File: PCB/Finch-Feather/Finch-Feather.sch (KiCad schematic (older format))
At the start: 37 parts, among them M1 STM32WB5MMGH6TR, Q1 DMP3125L-7, SW1 B3U-1000P, T1 20021121-00010C4LF, T2 TSW-112-07-G-S, T3 DX07S016JA1R1500, T4 TSW-116-07-L-S, T5 S2B-PH-SM4-TB(LF)(SN), U1 USBLC6-2P6, U2 TLV75533PDBVR, U3 MCP73831T-2ACI_OT

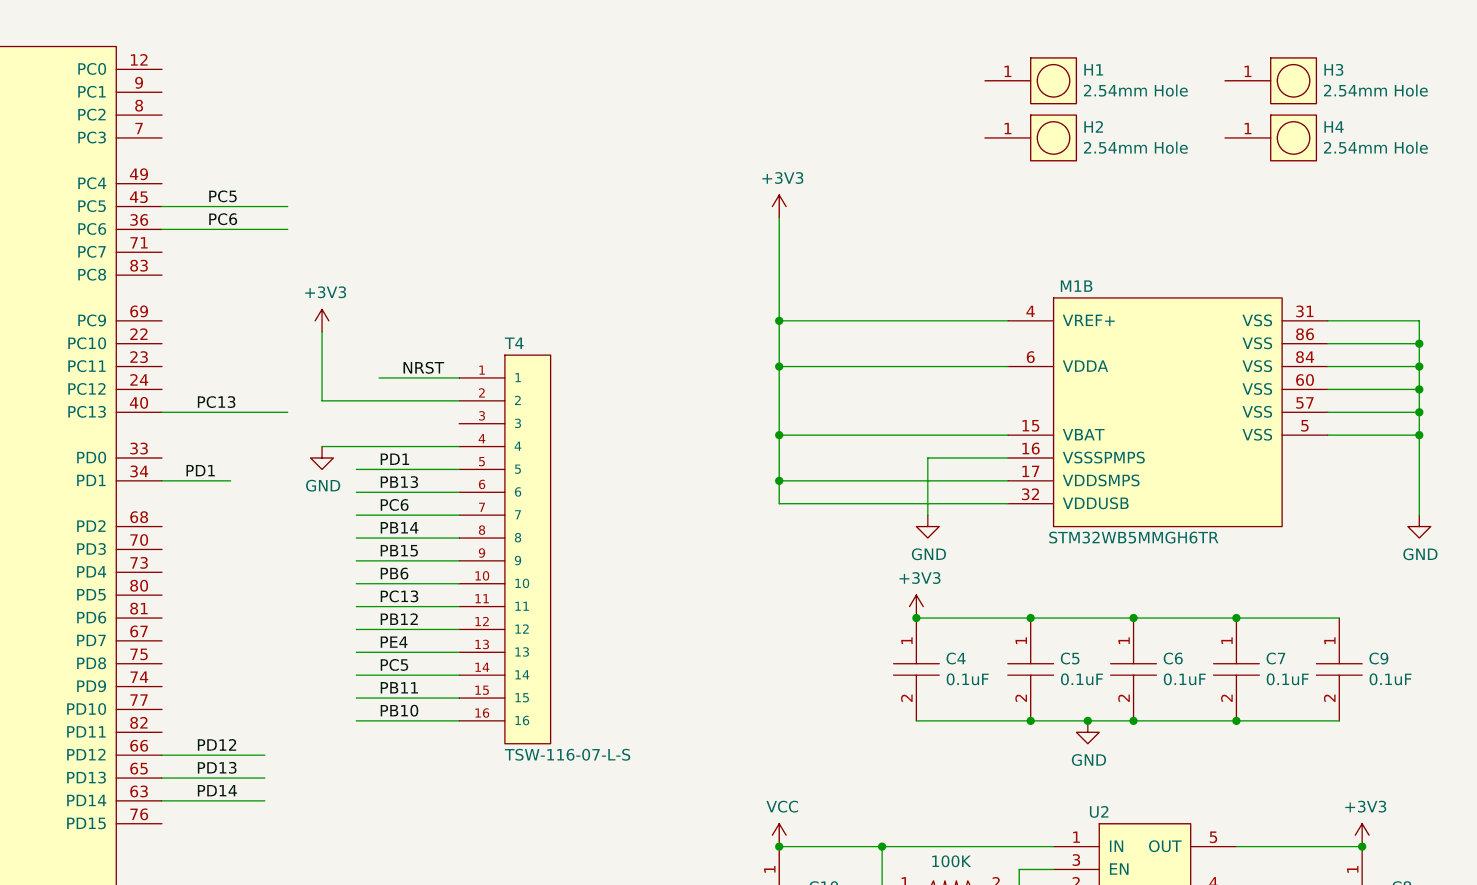
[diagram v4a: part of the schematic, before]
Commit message: Heavy PCB Rework
Reworked the Portion of the PCB around the ST RF module, signals re-chosen for 3 GPIOs to make the grounding conform more to the reference design recommendations.
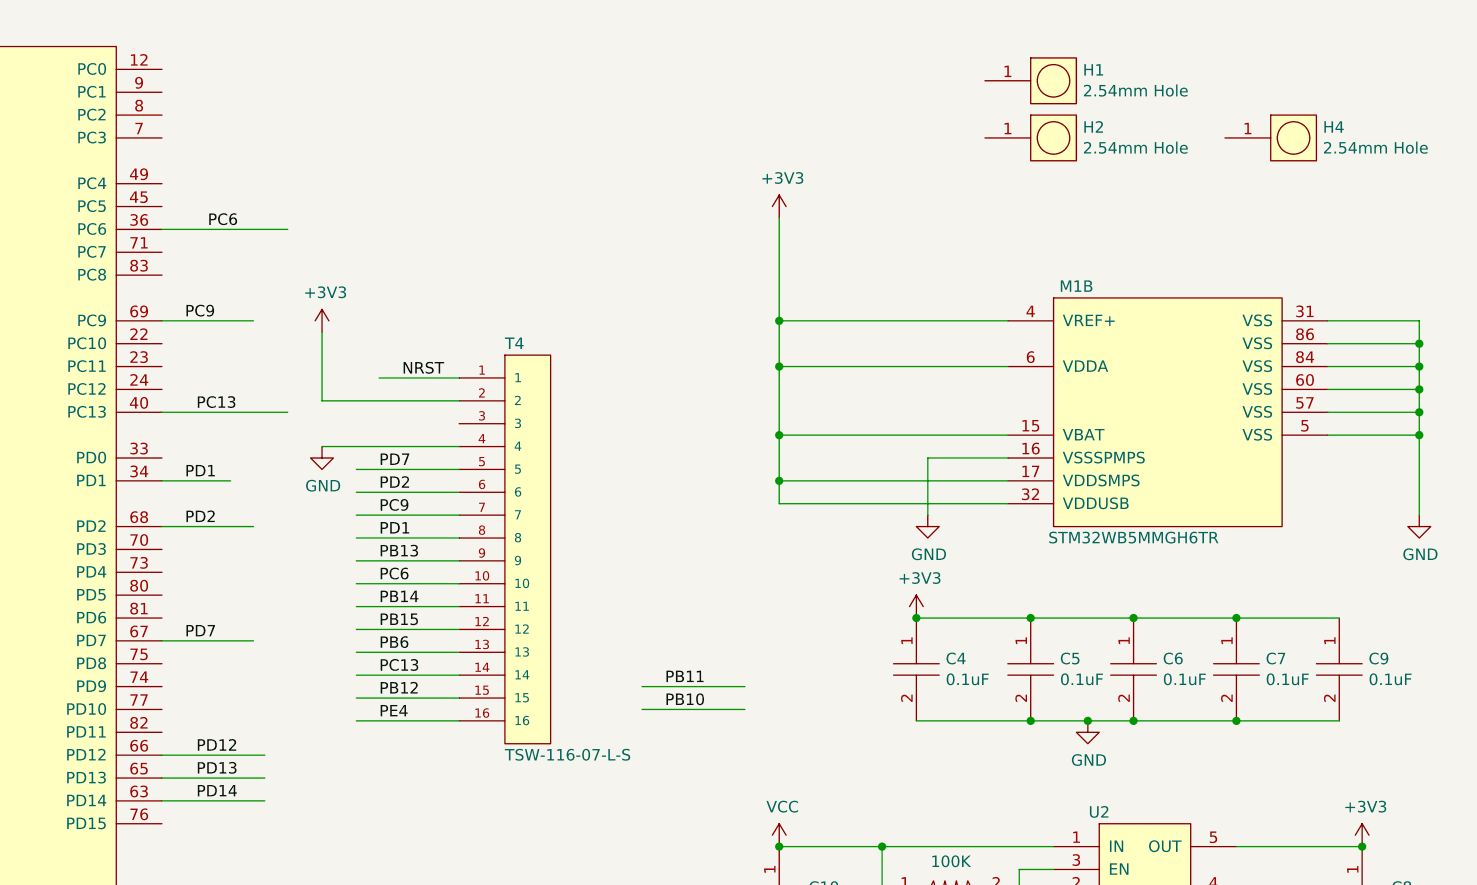
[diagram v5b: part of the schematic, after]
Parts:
- removed H3: 2.54mm_PLT_Hole, AVR-KiCAD-Lib-Holes_Fasteners:2.54mm_PLT_Hole, symbol AVR-KiCAD-Lib-Holes_Fasteners:2.54mm_PLT_Hole
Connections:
- net labels added: PC9, PD2, PD7
- net labels removed: PC5
- wire segments 171 -> 175
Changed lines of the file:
@@
-$EndComp
-$Comp
-L AVR-KiCAD-Lib-Holes_Fasteners:2.54mm_PLT_Hole H3
-U 1 1 608C5DF9
-P 10400 900
-F 0 "H3" H 10628 946 50  0000 L CNN
-F 1 "2.54mm_PLT_Hole" H 10450 1100 50  0001 C CNN
-F 2 "AVR-KiCAD-Lib-Holes_Fasteners:2.54mm_PLT_Hole" H 10400 900 50  0001 C CNN
-F 3 "" H 10400 900 50  0001 C CNN
-F 4 "*" H 10500 1150 50  0001 C CNN "Cost QTY: 1"
-F 5 "*" H 10600 1250 50  0001 C CNN "Cost QTY: 1000"
-F 6 "*" H 10700 1350 50  0001 C CNN "Cost QTY: 2500"
-F 7 "*" H 10800 1450 50  0001 C CNN "Cost QTY: 5000"
-F 8 "*" H 10900 1550 50  0001 C CNN "Cost QTY: 10000"
-F 9 "*" H 11000 1650 50  0001 C CNN "MFR"
-F 10 "*" H 11100 1750 50  0001 C CNN "MFR#"
-F 11 "*" H 11200 1850 50  0001 C CNN "Vendor"
-F 12 "*" H 11300 1950 50  0001 C CNN "Vendor #"
-F 13 "*" H 11400 2050 50  0001 C CNN "Designer"
-F 14 "*" H 11500 2150 50  0001 C CNN "Height"
-F 15 "*" H 12600 3250 50  0001 C CNN "Date Created"
-F 16 "*" H 11600 2250 50  0001 C CNN "Date Modified"
-F 17 "*" H 11700 2350 50  0001 C CNN "Lead-Free ?"
-F 18 "*" H 11800 2450 50  0001 C CNN "RoHS Levels"
-F 19 "*" H 11900 2550 50  0001 C CNN "Mounting"
-F 20 "*" H 12000 2650 50  0001 C CNN "Pin Count #"
-F 21 "*" H 12100 2750 50  0001 C CNN "Status"
-F 22 "*" H 12200 2850 50  0001 C CNN "Tolerance"
-F 23 "*" H 12300 2950 50  0001 C CNN "Type"
-F 24 "*" H 12400 3050 50  0001 C CNN "Voltage"
-F 25 "*" H 12500 3200 50  0001 C CNN "Package"
-F 26 "2.54mm Hole" H 10628 855 50  0000 L CNN "_Value_"
-F 27 "*" H 12800 3500 50  0001 C CNN "Management_ID"
-F 28 "*" H 12800 3500 50  0001 C CNN "Description"
-	1    10400 900
-	1    0    0    -1
 $EndComp
 $Comp
@@
 PB10
 Wire Wire Line
-	6850 3700 6400 3700
-Text Label 6500 3700 0    50   ~ 0
+	8100 3650 7650 3650
+Text Label 7750 3650 0    50   ~ 0
 PB10
 Wire Wire Line
@@
 PB11
 Wire Wire Line
-	6850 3600 6400 3600
-Text Label 6500 3600 0    50   ~ 0
+	8100 3550 7650 3550
+Text Label 7750 3550 0    50   ~ 0
 PB11
-Text Label 5750 1450 0    50   ~ 0
-PC5
-Wire Wire Line
-	5550 1450 6100 1450
-Text Label 6500 3500 0    50   ~ 0
-PC5
-Wire Wire Line
-	6400 3500 6850 3500
 Wire Wire Line
 	5550 5050 6050 5050
@@
 PE4
 Wire Wire Line
-	6400 3400 6850 3400
-Text Label 6500 3400 0    50   ~ 0
+	6400 3700 6850 3700
+Text Label 6500 3700 0    50   ~ 0
 PE4
 Wire Wire Line
@@
 PB12
 Wire Wire Line
-	6850 3300 6400 3300
-Text Label 6500 3300 0    50   ~ 0
+	6850 3600 6400 3600
+Text Label 6500 3600 0    50   ~ 0
 PB12
 Wire Wire Line
@@
 PC13
 Wire Wire Line
-	6850 3200 6400 3200
-Text Label 6500 3200 0    50   ~ 0
+	6850 3500 6400 3500
+Text Label 6500 3500 0    50   ~ 0
 PC13
 Wire Wire Line
@@
 PB6
 Wire Wire Line
-	6850 3100 6400 3100
-Text Label 6500 3100 0    50   ~ 0
+	6850 3400 6400 3400
+Text Label 6500 3400 0    50   ~ 0
 PB6
 Wire Wire Line
@@
 PB15
 Wire Wire Line
-	6850 3000 6400 3000
-Text Label 6500 3000 0    50   ~ 0
+	6850 3300 6400 3300
+Text Label 6500 3300 0    50   ~ 0
 PB15
 Wire Wire Line
@@
 PB14
 Wire Wire Line
-	6850 2900 6400 2900
-Text Label 6500 2900 0    50   ~ 0
+	6850 3200 6400 3200
+Text Label 6500 3200 0    50   ~ 0
 PB14
 Wire Wire Line
@@
 PC6
 Wire Wire Line
-	6400 2800 6850 2800
-Text Label 6500 2800 0    50   ~ 0
+	6400 3100 6850 3100
+Text Label 6500 3100 0    50   ~ 0
 PC6
 Wire Wire Line
@@
 PB13
 Wire Wire Line
-	6400 2700 6850 2700
-Text Label 6500 2700 0    50   ~ 0
+	6400 3000 6850 3000
+Text Label 6500 3000 0    50   ~ 0
 PB13
 Wire Wire Line
@@
 PD1
 Wire Wire Line
-	6400 2600 6850 2600
-Text Label 6500 2600 0    50   ~ 0
+	6400 2900 6850 2900
+Text Label 6500 2900 0    50   ~ 0
 PD1
 Wire Wire Line
@@
 Wire Wire Line
 	9100 5450 9100 6250
+Wire Wire Line
+	5550 3350 5950 3350
+Text Label 5650 3350 0    50   ~ 0
+PD7
+Wire Wire Line
+	6400 2600 6850 2600
+Text Label 6500 2600 0    50   ~ 0
+PD7
+Wire Wire Line
+	5550 2850 5950 2850
+Text Label 5650 2850 0    50   ~ 0
+PD2
+Wire Wire Line
+	6400 2700 6850 2700
+Text Label 6500 2700 0    50   ~ 0
+PD2
+Wire Wire Line
+	5550 1950 5950 1950
+Text Label 5650 1950 0    50   ~ 0
+PC9
+Wire Wire Line
+	6400 2800 6850 2800
+Text Label 6500 2800 0    50   ~ 0
+PC9
 $EndSCHEMATC

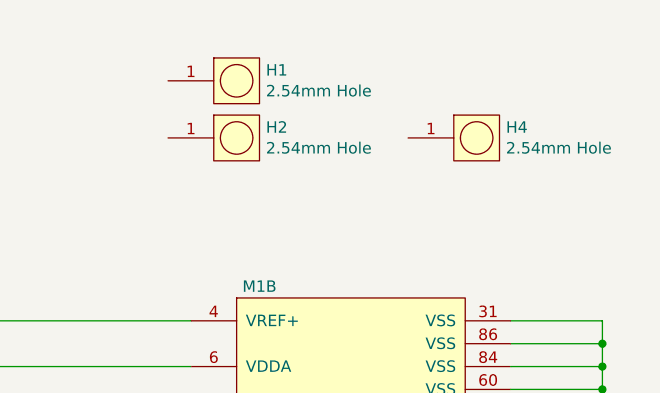
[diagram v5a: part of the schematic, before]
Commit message: Prefab changes
minor adjustments, removal of screw holes, and additional via stitching
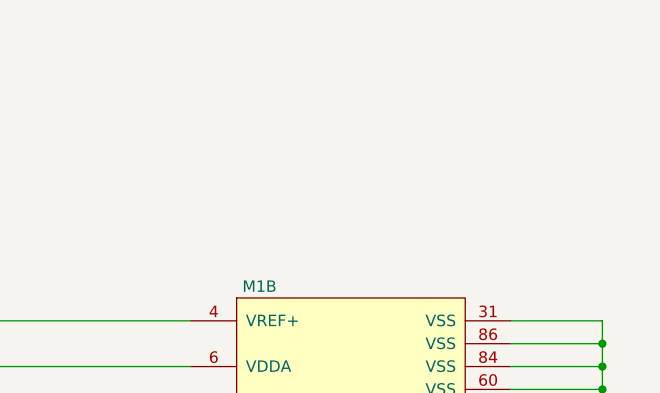
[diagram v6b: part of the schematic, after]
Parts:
- removed H1, H2, H4: 2.54mm_PLT_Hole, AVR-KiCAD-Lib-Holes_Fasteners:2.54mm_PLT_Hole, symbol AVR-KiCAD-Lib-Holes_Fasteners:2.54mm_PLT_Hole
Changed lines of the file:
@@
-$EndComp
-$Comp
-L AVR-KiCAD-Lib-Holes_Fasteners:2.54mm_PLT_Hole H1
-U 1 1 608C1076
-P 9350 900
-F 0 "H1" H 9578 946 50  0000 L CNN
-F 1 "2.54mm_PLT_Hole" H 9400 1100 50  0001 C CNN
-F 2 "AVR-KiCAD-Lib-Holes_Fasteners:2.54mm_PLT_Hole" H 9350 900 50  0001 C CNN
-F 3 "" H 9350 900 50  0001 C CNN
-F 4 "*" H 9450 1150 50  0001 C CNN "Cost QTY: 1"
-F 5 "*" H 9550 1250 50  0001 C CNN "Cost QTY: 1000"
-F 6 "*" H 9650 1350 50  0001 C CNN "Cost QTY: 2500"
-F 7 "*" H 9750 1450 50  0001 C CNN "Cost QTY: 5000"
-F 8 "*" H 9850 1550 50  0001 C CNN "Cost QTY: 10000"
-F 9 "*" H 9950 1650 50  0001 C CNN "MFR"
-F 10 "*" H 10050 1750 50  0001 C CNN "MFR#"
-F 11 "*" H 10150 1850 50  0001 C CNN "Vendor"
-F 12 "*" H 10250 1950 50  0001 C CNN "Vendor #"
-F 13 "*" H 10350 2050 50  0001 C CNN "Designer"
-F 14 "*" H 10450 2150 50  0001 C CNN "Height"
-F 15 "*" H 11550 3250 50  0001 C CNN "Date Created"
-F 16 "*" H 10550 2250 50  0001 C CNN "Date Modified"
-F 17 "*" H 10650 2350 50  0001 C CNN "Lead-Free ?"
-F 18 "*" H 10750 2450 50  0001 C CNN "RoHS Levels"
-F 19 "*" H 10850 2550 50  0001 C CNN "Mounting"
-F 20 "*" H 10950 2650 50  0001 C CNN "Pin Count #"
-F 21 "*" H 11050 2750 50  0001 C CNN "Status"
-F 22 "*" H 11150 2850 50  0001 C CNN "Tolerance"
-F 23 "*" H 11250 2950 50  0001 C CNN "Type"
-F 24 "*" H 11350 3050 50  0001 C CNN "Voltage"
-F 25 "*" H 11450 3200 50  0001 C CNN "Package"
-F 26 "2.54mm Hole" H 9578 855 50  0000 L CNN "_Value_"
-F 27 "*" H 11750 3500 50  0001 C CNN "Management_ID"
-F 28 "*" H 11750 3500 50  0001 C CNN "Description"
-	1    9350 900
-	1    0    0    -1
-$EndComp
-$Comp
-L AVR-KiCAD-Lib-Holes_Fasteners:2.54mm_PLT_Hole H2
-U 1 1 608C3B0F
-P 9350 1150
-F 0 "H2" H 9578 1196 50  0000 L CNN
-F 1 "2.54mm_PLT_Hole" H 9400 1350 50  0001 C CNN
-F 2 "AVR-KiCAD-Lib-Holes_Fasteners:2.54mm_PLT_Hole" H 9350 1150 50  0001 C CNN
-F 3 "" H 9350 1150 50  0001 C CNN
-F 4 "*" H 9450 1400 50  0001 C CNN "Cost QTY: 1"
-F 5 "*" H 9550 1500 50  0001 C CNN "Cost QTY: 1000"
-F 6 "*" H 9650 1600 50  0001 C CNN "Cost QTY: 2500"
-F 7 "*" H 9750 1700 50  0001 C CNN "Cost QTY: 5000"
-F 8 "*" H 9850 1800 50  0001 C CNN "Cost QTY: 10000"
-F 9 "*" H 9950 1900 50  0001 C CNN "MFR"
-F 10 "*" H 10050 2000 50  0001 C CNN "MFR#"
-F 11 "*" H 10150 2100 50  0001 C CNN "Vendor"
-F 12 "*" H 10250 2200 50  0001 C CNN "Vendor #"
-F 13 "*" H 10350 2300 50  0001 C CNN "Designer"
-F 14 "*" H 10450 2400 50  0001 C CNN "Height"
-F 15 "*" H 11550 3500 50  0001 C CNN "Date Created"
-F 16 "*" H 10550 2500 50  0001 C CNN "Date Modified"
-F 17 "*" H 10650 2600 50  0001 C CNN "Lead-Free ?"
-F 18 "*" H 10750 2700 50  0001 C CNN "RoHS Levels"
-F 19 "*" H 10850 2800 50  0001 C CNN "Mounting"
-F 20 "*" H 10950 2900 50  0001 C CNN "Pin Count #"
-F 21 "*" H 11050 3000 50  0001 C CNN "Status"
-F 22 "*" H 11150 3100 50  0001 C CNN "Tolerance"
-F 23 "*" H 11250 3200 50  0001 C CNN "Type"
-F 24 "*" H 11350 3300 50  0001 C CNN "Voltage"
-F 25 "*" H 11450 3450 50  0001 C CNN "Package"
-F 26 "2.54mm Hole" H 9578 1105 50  0000 L CNN "_Value_"
-F 27 "*" H 11750 3750 50  0001 C CNN "Management_ID"
-F 28 "*" H 11750 3750 50  0001 C CNN "Description"
-	1    9350 1150
-	1    0    0    -1
-$EndComp
-$Comp
-L AVR-KiCAD-Lib-Holes_Fasteners:2.54mm_PLT_Hole H4
-U 1 1 608C46AE
-P 10400 1150
-F 0 "H4" H 10628 1196 50  0000 L CNN
-F 1 "2.54mm_PLT_Hole" H 10450 1350 50  0001 C CNN
-F 2 "AVR-KiCAD-Lib-Holes_Fasteners:2.54mm_PLT_Hole" H 10400 1150 50  0001 C CNN
-F 3 "" H 10400 1150 50  0001 C CNN
-F 4 "*" H 10500 1400 50  0001 C CNN "Cost QTY: 1"
-F 5 "*" H 10600 1500 50  0001 C CNN "Cost QTY: 1000"
-F 6 "*" H 10700 1600 50  0001 C CNN "Cost QTY: 2500"
-F 7 "*" H 10800 1700 50  0001 C CNN "Cost QTY: 5000"
-F 8 "*" H 10900 1800 50  0001 C CNN "Cost QTY: 10000"
-F 9 "*" H 11000 1900 50  0001 C CNN "MFR"
-F 10 "*" H 11100 2000 50  0001 C CNN "MFR#"
-F 11 "*" H 11200 2100 50  0001 C CNN "Vendor"
-F 12 "*" H 11300 2200 50  0001 C CNN "Vendor #"
-F 13 "*" H 11400 2300 50  0001 C CNN "Designer"
-F 14 "*" H 11500 2400 50  0001 C CNN "Height"
-F 15 "*" H 12600 3500 50  0001 C CNN "Date Created"
-F 16 "*" H 11600 2500 50  0001 C CNN "Date Modified"
-F 17 "*" H 11700 2600 50  0001 C CNN "Lead-Free ?"
-F 18 "*" H 11800 2700 50  0001 C CNN "RoHS Levels"
-F 19 "*" H 11900 2800 50  0001 C CNN "Mounting"
-F 20 "*" H 12000 2900 50  0001 C CNN "Pin Count #"
-F 21 "*" H 12100 3000 50  0001 C CNN "Status"
-F 22 "*" H 12200 3100 50  0001 C CNN "Tolerance"
-F 23 "*" H 12300 3200 50  0001 C CNN "Type"
-F 24 "*" H 12400 3300 50  0001 C CNN "Voltage"
-F 25 "*" H 12500 3450 50  0001 C CNN "Package"
-F 26 "2.54mm Hole" H 10628 1105 50  0000 L CNN "_Value_"
-F 27 "*" H 12800 3750 50  0001 C CNN "Management_ID"
-F 28 "*" H 12800 3750 50  0001 C CNN "Description"
-	1    10400 1150
-	1    0    0    -1
 $EndComp
 $Comp
